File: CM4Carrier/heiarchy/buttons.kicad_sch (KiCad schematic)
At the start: 69 parts, among them J2 Conn_01x04_Female, SW1 SW_Push, SW10 SW_Push, SW11 SW_Push, SW2 SW_Push, SW3 SW_Push, SW4 SW_Push, SW5 SW_Push, SW6 SW_Push, SW7 SW_Push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

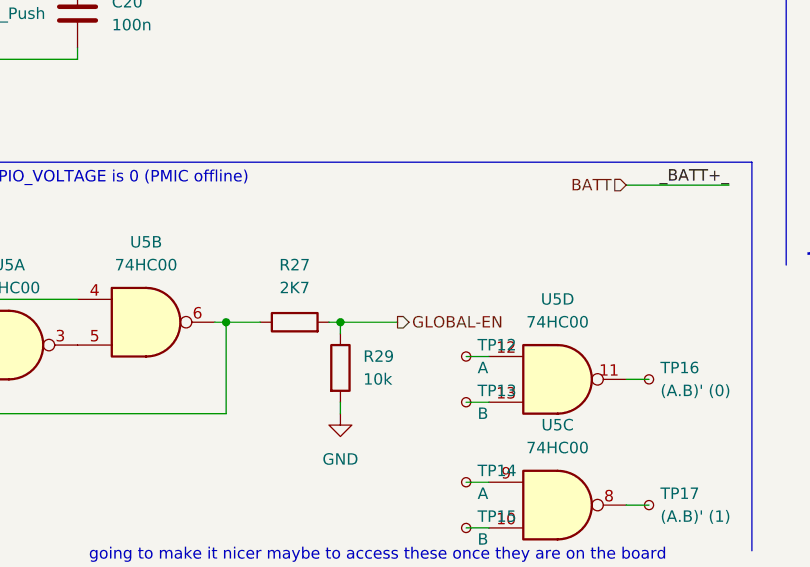
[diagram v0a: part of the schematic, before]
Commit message: PCB work
Home-stretch! Remaining things:
- Forgot Headphone jack / audio in design - add.
- route power supply (aaaaa)
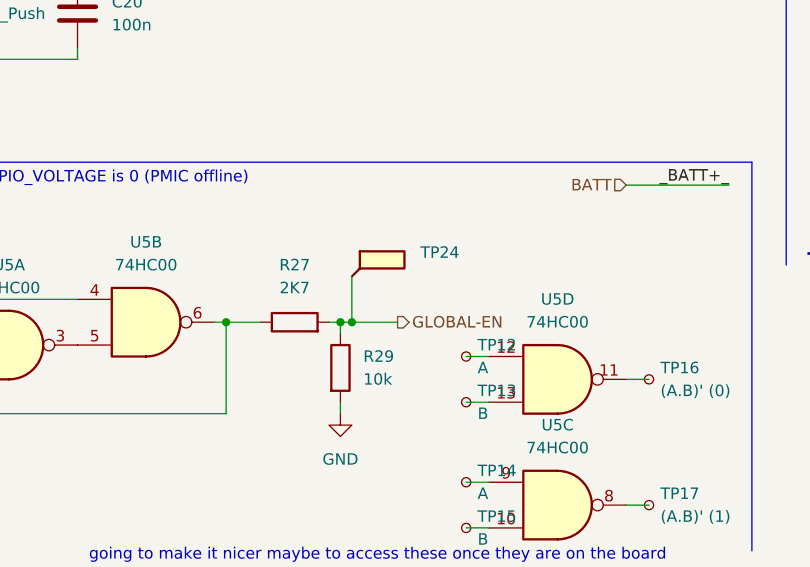
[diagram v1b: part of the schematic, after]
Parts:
- added TP24: (no value), symbol Connector:TestPoint_Flag
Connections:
- net GLOBAL-EN: now also TP24.1
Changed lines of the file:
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@@
   (junction (at 88.9 40.64) (diameter 0) (color 0 0 0 0)
   )
+  (junction (at 129.54 171.45) (diameter 0) (color 0 0 0 0)
+  )
   (junction (at 60.96 173.99) (diameter 0) (color 0 0 0 0)
   )
@@
     (stroke (width 0) (type default) (color 0 0 0 0))
   )
+  (wire (pts (xy 128.27 171.45) (xy 129.54 171.45))
+    (stroke (width 0) (type default) (color 0 0 0 0))
+  )
   (wire (pts (xy 88.9 40.64) (xy 88.9 39.37))
     (stroke (width 0) (type default) (color 0 0 0 0))
@@
     (stroke (width 0) (type default) (color 0 0 0 0))
   )
+  (wire (pts (xy 129.54 171.45) (xy 134.62 171.45))
+    (stroke (width 0) (type default) (color 0 0 0 0))
+  )
   (wire (pts (xy 111.76 76.2) (xy 114.3 76.2))
     (stroke (width 0) (type default) (color 0 0 0 0))
@@
     (stroke (width 0) (type default) (color 0 0 0 0))
   )
+  (wire (pts (xy 129.54 166.37) (xy 129.54 171.45))
+    (stroke (width 0) (type default) (color 0 0 0 0))
+  )
   (wire (pts (xy 142.24 189.23) (xy 144.78 189.23))
     (stroke (width 0) (type default) (color 0 0 0 0))
@@
   )
   (wire (pts (xy 204.47 45.72) (xy 204.47 46.99))
-    (stroke (width 0) (type default) (color 0 0 0 0))
-  )
-  (wire (pts (xy 128.27 171.45) (xy 134.62 171.45))
     (stroke (width 0) (type default) (color 0 0 0 0))
   )
@@
     (pin "1")
     (pin "2")
+  )
+  (symbol (lib_id "Connector:TestPoint_Flag") (at 129.54 166.37 0) (unit 1)
+    (in_bom yes) (on_board yes) (fields_autoplaced)
+    (property "Reference" "TP24" (id 0) (at 137.16 163.7029 0)
+      (effects (font (size 1.27 1.27)) (justify left))
+    )
+    (property "Value" "" (id 1) (at 137.16 166.2429 0)
+      (effects (font (size 1.27 1.27)) (justify left))
+    )
+    (property "Footprint" "" (id 2) (at 134.62 166.37 0)
+      (effects (font (size 1.27 1.27)) hide)
+    )
+    (property "Datasheet" "~" (id 3) (at 134.62 166.37 0)
+      (effects (font (size 1.27 1.27)) hide)
+    )
+    (pin "1")
   )
   (symbol (lib_id "Connector:TestPoint_Small") (at 142.24 189.23 0) (unit 1)
@@
       (effects (font (size 1.27 1.27)) hide)
     )
+    (pin "1")
+    (pin "2")
+    (pin "3")
+    (pin "4")
+    (pin "5")
+    (pin "6")
+    (pin "10")
+    (pin "8")
+    (pin "9")
+    (pin "11")
+    (pin "12")
+    (pin "13")
     (pin "14")
     (pin "7")
@@
       (effects (font (size 1.27 1.27)) hide)
     )
+    (pin "1")
+    (pin "2")
+    (pin "3")
     (pin "4")
     (pin "5")
     (pin "6")
+    (pin "10")
+    (pin "8")
+    (pin "9")
+    (pin "11")
+    (pin "12")
+    (pin "13")
+    (pin "14")
+    (pin "7")
   )
   (symbol (lib_id "Switch:SW_Push") (at 247.65 72.39 90) (unit 1)
@@
       (effects (font (size 1.27 1.27)) hide)
     )
+    (pin "1")
+    (pin "2")
+    (pin "3")
+    (pin "4")
+    (pin "5")
+    (pin "6")
     (pin "10")
     (pin "8")
     (pin "9")
+    (pin "11")
+    (pin "12")
+    (pin "13")
+    (pin "14")
+    (pin "7")
   )
   (symbol (lib_id "Connector:TestPoint_Flag") (at 134.62 63.5 0) (unit 1)
@@
       (effects (font (size 1.27 1.27)) hide)
     )
+    (pin "1")
+    (pin "2")
+    (pin "3")
+    (pin "4")
+    (pin "5")
+    (pin "6")
+    (pin "10")
+    (pin "8")
+    (pin "9")
     (pin "11")
     (pin "12")
     (pin "13")
+    (pin "14")
+    (pin "7")
   )
   (symbol (lib_id "Device:C") (at 88.9 97.79 0) (unit 1)
@@
     (pin "2")
     (pin "3")
+    (pin "4")
+    (pin "5")
+    (pin "6")
+    (pin "10")
+    (pin "8")
+    (pin "9")
+    (pin "11")
+    (pin "12")
+    (pin "13")
+    (pin "14")
+    (pin "7")
   )
 )

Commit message: LAYOUT DONE!!
:)
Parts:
- TP24: value (none) -> TP-GLOBALEN; footprint (none) -> TestPoint:TestPoint_THTPad_1.0x1.0mm_Drill0.5mm
- U5: value 74HC00 -> (none); footprint Package_DIP:DIP-14_W7.62mm_Socket_LongPads -> (none)
- U6: value MCP3002 -> (none); footprint Package_DIP:DIP-8_W7.62mm_LongPads -> (none)
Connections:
- net _BATT+ is gone; now on net BATT: R17.2, R19.2, U5.14 (VCC)
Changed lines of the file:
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@@
     (effects (font (size 2.54 2.54)) (justify left bottom))
   )
-  (label "_BATT+_" (at 171.45 156.21 180)
+  (label "BATT_S" (at 171.45 156.21 180)
     (effects (font (size 1.27 1.27)) (justify right bottom))
   )
@@
     (effects (font (size 1.27 1.27)) (justify left bottom))
   )
-  (label "_BATT+" (at 20.32 160.02 0)
+  (label "BATT_S" (at 20.32 160.02 0)
     (effects (font (size 1.27 1.27)) (justify left bottom))
   )
@@
     (effects (font (size 1.27 1.27)) (justify right bottom))
   )
-  (label "_BATT+" (at 69.85 158.75 180)
+  (label "BATT_S" (at 69.85 158.75 180)
     (effects (font (size 1.27 1.27)) (justify right bottom))
   )
@@
       (effects (font (size 1.27 1.27)) (justify left))
     )
-    (property "Value" "" (id 1) (at 137.16 166.2429 0)
-      (effects (font (size 1.27 1.27)) (justify left))
-    )
-    (property "Footprint" "" (id 2) (at 134.62 166.37 0)
+    (property "Value" "TP-GLOBALEN" (id 1) (at 137.16 166.2429 0)
+      (effects (font (size 1.27 1.27)) (justify left))
+    )
+    (property "Footprint" "TestPoint:TestPoint_THTPad_1.0x1.0mm_Drill0.5mm" (id 2) (at 134.62 166.37 0)
       (effects (font (size 1.27 1.27)) hide)
     )
@@
       (effects (font (size 1.27 1.27)) (justify left))
     )
-    (property "Value" "74HC00" (id 1) (at 31.75 175.2599 0)
-      (effects (font (size 1.27 1.27)) (justify left))
-    )
-    (property "Footprint" "Package_DIP:DIP-14_W7.62mm_Socket_LongPads" (id 2) (at 25.4 173.99 0)
-      (effects (font (size 1.27 1.27)) hide)
-    )
+    (property "Value" "" (id 1) (at 31.75 175.2599 0)
+      (effects (font (size 1.27 1.27)) (justify left))
+    )
+    (property "Footprint" "" (id 2) (at 25.4 173.99 0))
     (property "Datasheet" "http://www.ti.com/lit/gpn/sn74hc00" (id 3) (at 25.4 173.99 0)
       (effects (font (size 1.27 1.27)) hide)
@@
     (in_bom yes) (on_board yes) (fields_autoplaced)
     (property "Reference" "U5" (id 0) (at 106.68 162.56 0))
-    (property "Value" "74HC00" (id 1) (at 106.68 165.1 0))
-    (property "Footprint" "Package_DIP:DIP-14_W7.62mm_Socket_LongPads" (id 2) (at 106.68 171.45 0)
+    (property "Value" "" (id 1) (at 106.68 165.1 0))
+    (property "Footprint" "" (id 2) (at 106.68 171.45 0)
       (effects (font (size 1.27 1.27)) hide)
     )
@@
       (effects (font (size 1.27 1.27)) (justify left))
     )
-    (property "Value" "MCP3002" (id 1) (at 258.5594 116.84 0)
-      (effects (font (size 1.27 1.27)) (justify left))
-    )
-    (property "Footprint" "Package_DIP:DIP-8_W7.62mm_LongPads" (id 2) (at 256.54 132.08 0)
+    (property "Value" "" (id 1) (at 258.5594 116.84 0)
+      (effects (font (size 1.27 1.27)) (justify left))
+    )
+    (property "Footprint" "" (id 2) (at 256.54 132.08 0)
       (effects (font (size 1.27 1.27)) hide)
     )
@@
     (in_bom yes) (on_board yes) (fields_autoplaced)
     (property "Reference" "U5" (id 0) (at 152.4 182.88 0))
-    (property "Value" "74HC00" (id 1) (at 152.4 185.42 0))
-    (property "Footprint" "Package_DIP:DIP-14_W7.62mm_Socket_LongPads" (id 2) (at 152.4 191.77 0)
+    (property "Value" "" (id 1) (at 152.4 185.42 0))
+    (property "Footprint" "" (id 2) (at 152.4 191.77 0)
       (effects (font (size 1.27 1.27)) hide)
     )
@@
     (in_bom yes) (on_board yes) (fields_autoplaced)
     (property "Reference" "U5" (id 0) (at 152.4 168.91 0))
-    (property "Value" "74HC00" (id 1) (at 152.4 171.45 0))
-    (property "Footprint" "Package_DIP:DIP-14_W7.62mm_Socket_LongPads" (id 2) (at 152.4 177.8 0)
+    (property "Value" "" (id 1) (at 152.4 171.45 0))
+    (property "Footprint" "" (id 2) (at 152.4 177.8 0)
       (effects (font (size 1.27 1.27)) hide)
     )
@@
     (in_bom yes) (on_board yes) (fields_autoplaced)
     (property "Reference" "U5" (id 0) (at 91.44 165.1 0))
-    (property "Value" "74HC00" (id 1) (at 91.44 167.64 0))
-    (property "Footprint" "Package_DIP:DIP-14_W7.62mm_Socket_LongPads" (id 2) (at 91.44 173.99 0)
-      (effects (font (size 1.27 1.27)) hide)
-    )
+    (property "Value" "" (id 1) (at 91.44 167.64 0))
+    (property "Footprint" "" (id 2) (at 91.44 173.99 0)
+      (effects (font (size 1.27 1.27)) hide)
+    )

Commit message: fuseeeeeeeeeeeeeeeeeeeeeeeeeeeeeeeeeeeeeeeeeee
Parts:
- U5: value (none) -> 74HC00; footprint (none) -> Package_SO:SOIC-14_3.9x8.7mm_P1.27mm
- U6: value (none) -> MCP3002; footprint (none) -> Package_SO:TSSOP-8_4.4x3mm_P0.65mm
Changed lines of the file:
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@@
       (effects (font (size 1.27 1.27)) (justify left))
     )
-    (property "Value" "" (id 1) (at 31.75 175.2599 0)
-      (effects (font (size 1.27 1.27)) (justify left))
-    )
-    (property "Footprint" "" (id 2) (at 25.4 173.99 0))
+    (property "Value" "74HC00" (id 1) (at 31.75 175.2599 0)
+      (effects (font (size 1.27 1.27)) (justify left))
+    )
+    (property "Footprint" "Package_SO:SOIC-14_3.9x8.7mm_P1.27mm" (id 2) (at 25.4 173.99 0))
     (property "Datasheet" "http://www.ti.com/lit/gpn/sn74hc00" (id 3) (at 25.4 173.99 0)
       (effects (font (size 1.27 1.27)) hide)
@@
     (in_bom yes) (on_board yes) (fields_autoplaced)
     (property "Reference" "U5" (id 0) (at 106.68 162.56 0))
-    (property "Value" "" (id 1) (at 106.68 165.1 0))
-    (property "Footprint" "" (id 2) (at 106.68 171.45 0)
+    (property "Value" "74HC00" (id 1) (at 106.68 165.1 0))
+    (property "Footprint" "Package_SO:SOIC-14_3.9x8.7mm_P1.27mm" (id 2) (at 106.68 171.45 0)
       (effects (font (size 1.27 1.27)) hide)
     )
@@
       (effects (font (size 1.27 1.27)) (justify left))
     )
-    (property "Value" "" (id 1) (at 258.5594 116.84 0)
-      (effects (font (size 1.27 1.27)) (justify left))
-    )
-    (property "Footprint" "" (id 2) (at 256.54 132.08 0)
+    (property "Value" "MCP3002" (id 1) (at 258.5594 116.84 0)
+      (effects (font (size 1.27 1.27)) (justify left))
+    )
+    (property "Footprint" "Package_SO:TSSOP-8_4.4x3mm_P0.65mm" (id 2) (at 256.54 132.08 0)
       (effects (font (size 1.27 1.27)) hide)
     )
@@
     (in_bom yes) (on_board yes) (fields_autoplaced)
     (property "Reference" "U5" (id 0) (at 152.4 182.88 0))
-    (property "Value" "" (id 1) (at 152.4 185.42 0))
-    (property "Footprint" "" (id 2) (at 152.4 191.77 0)
+    (property "Value" "74HC00" (id 1) (at 152.4 185.42 0))
+    (property "Footprint" "Package_SO:SOIC-14_3.9x8.7mm_P1.27mm" (id 2) (at 152.4 191.77 0)
       (effects (font (size 1.27 1.27)) hide)
     )
@@
     (in_bom yes) (on_board yes) (fields_autoplaced)
     (property "Reference" "U5" (id 0) (at 152.4 168.91 0))
-    (property "Value" "" (id 1) (at 152.4 171.45 0))
-    (property "Footprint" "" (id 2) (at 152.4 177.8 0)
+    (property "Value" "74HC00" (id 1) (at 152.4 171.45 0))
+    (property "Footprint" "Package_SO:SOIC-14_3.9x8.7mm_P1.27mm" (id 2) (at 152.4 177.8 0)
       (effects (font (size 1.27 1.27)) hide)
     )
@@
     (in_bom yes) (on_board yes) (fields_autoplaced)
     (property "Reference" "U5" (id 0) (at 91.44 165.1 0))
-    (property "Value" "" (id 1) (at 91.44 167.64 0))
-    (property "Footprint" "" (id 2) (at 91.44 173.99 0)
-      (effects (font (size 1.27 1.27)) hide)
-    )
+    (property "Value" "74HC00" (id 1) (at 91.44 167.64 0))
+    (property "Footprint" "Package_SO:SOIC-14_3.9x8.7mm_P1.27mm" (id 2) (at 91.44 173.99 0)
+      (effects (font (size 1.27 1.27)) hide)
+    )

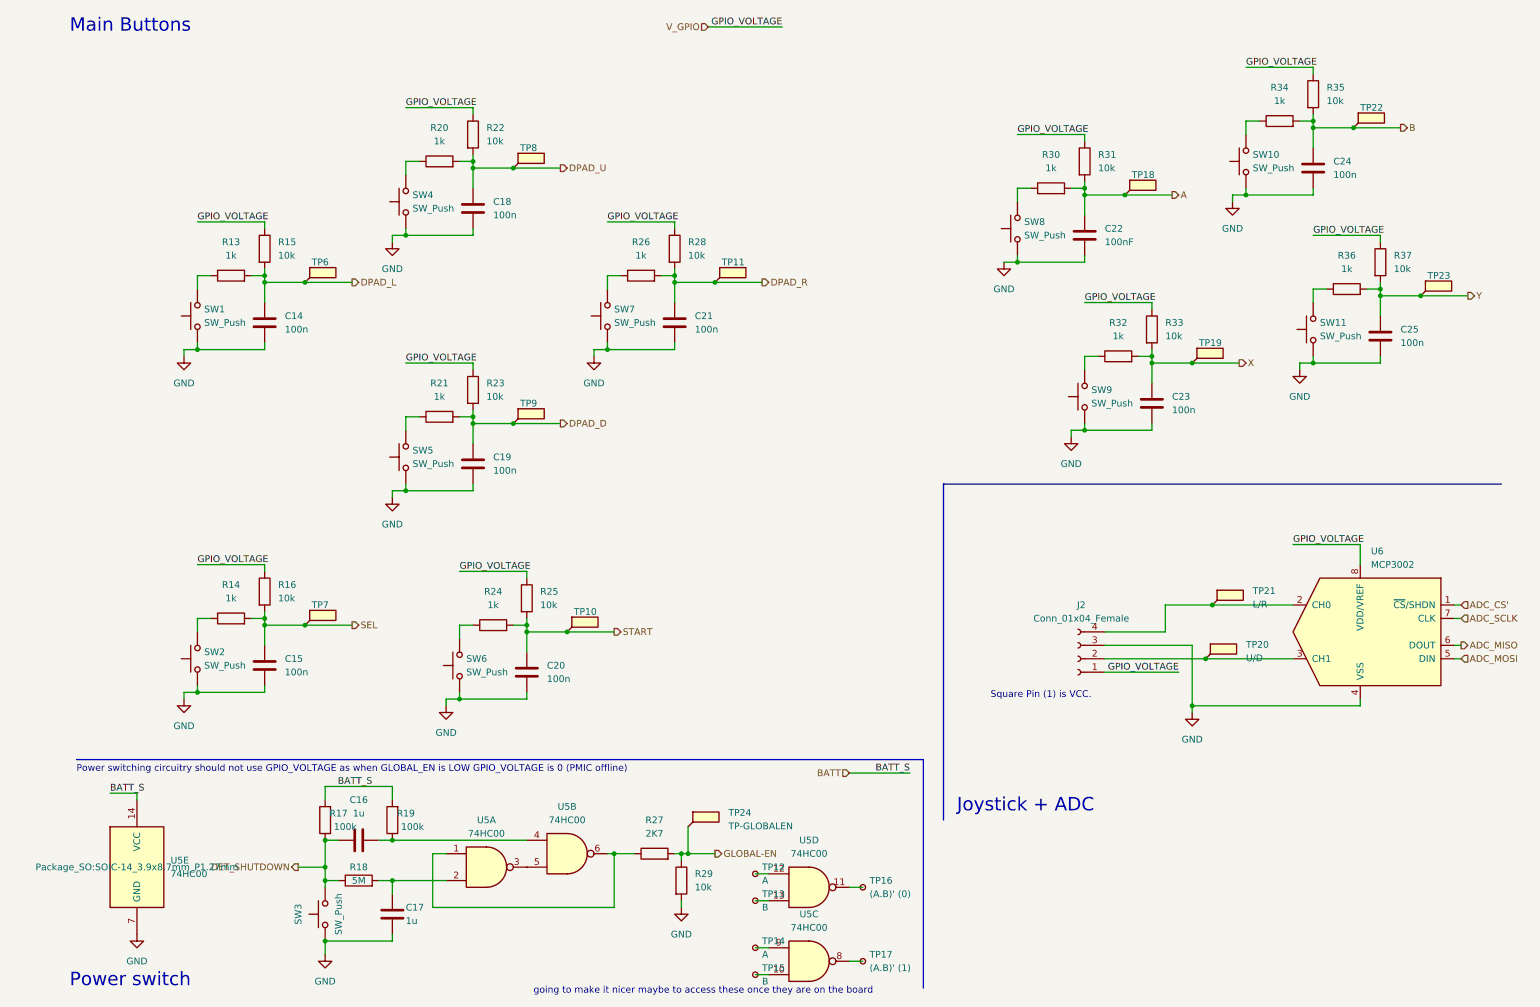
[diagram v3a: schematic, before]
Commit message: add buttons
need to adjust 3d model for buttons and add them to pcb... forgot about these.
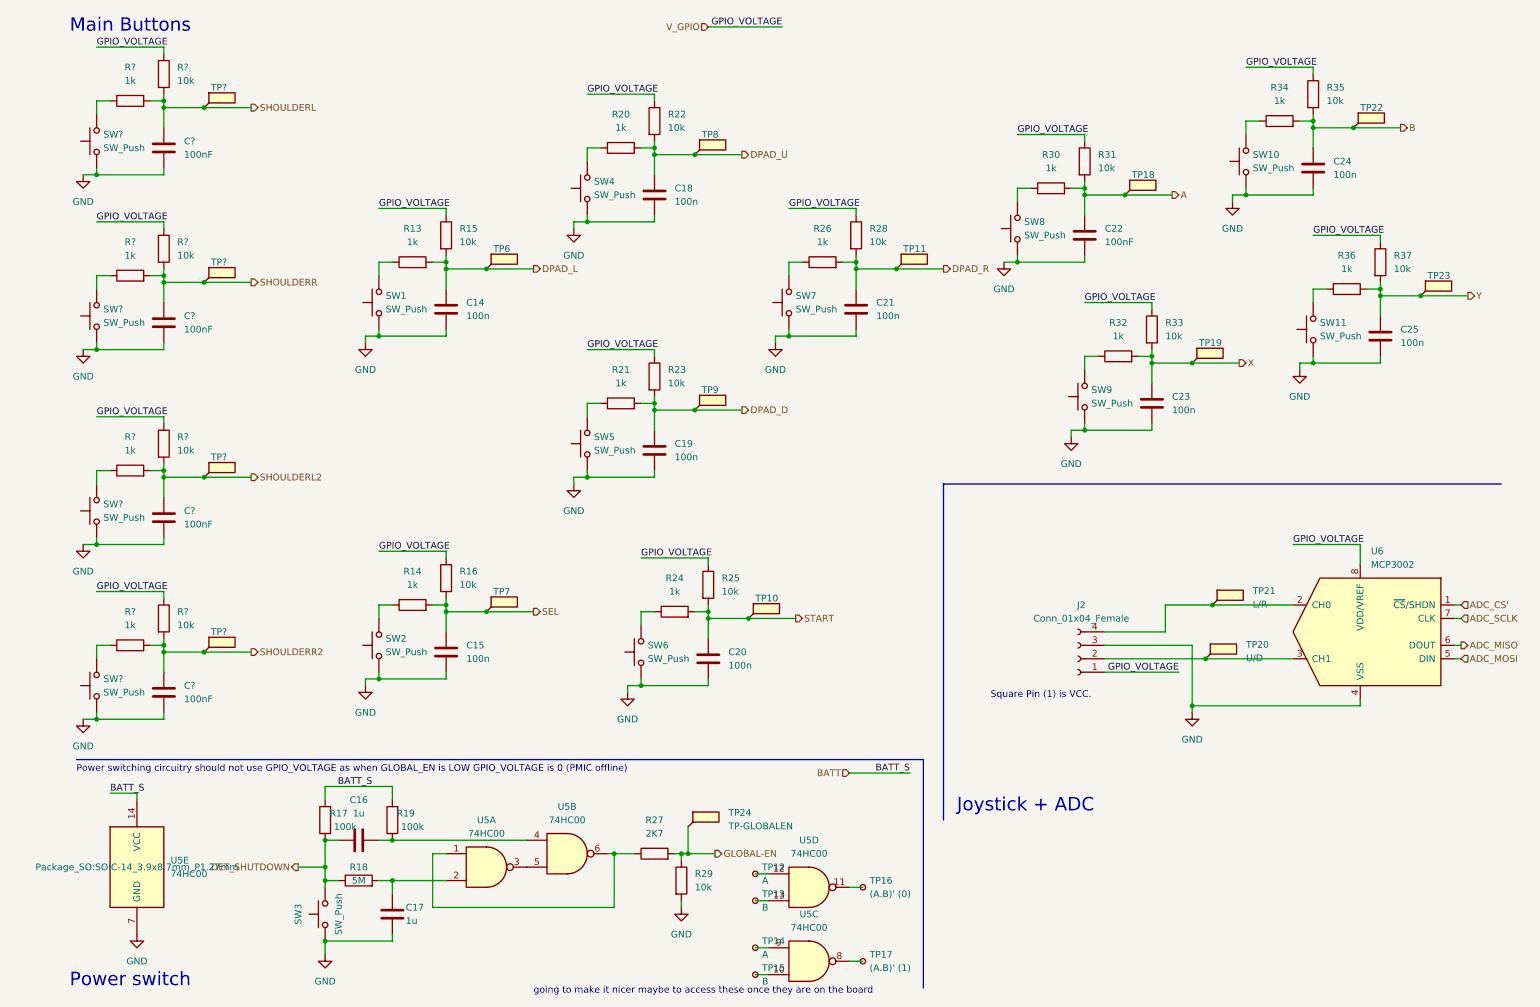
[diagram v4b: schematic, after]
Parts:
- added C? (x4): 100nF, Capacitor_SMD:C_0805_2012Metric_Pad1.18x1.45mm_HandSolder, symbol Device:C
- added R? (x4): 10k, Resistor_SMD:R_0805_2012Metric_Pad1.20x1.40mm_HandSolder, symbol Device:R
- added R? (x4): 1k, Resistor_SMD:R_0805_2012Metric_Pad1.20x1.40mm_HandSolder, symbol Device:R
- added SW? (x4): SW_Push, CM4IO:SW_PTS526_SMG15_SMTR2_LFS, symbol Switch:SW_Push
- added TP? (x4): A, TestPoint:TestPoint_THTPad_1.0x1.0mm_Drill0.5mm, symbol Connector:TestPoint_Flag
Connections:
- net GND: now also C?.2, C?.2, C?.2, C?.2, SW?.1, SW?.1, SW?.1, SW?.1
- net V_GPIO: now also R?.1, R?.1, R?.1, R?.1
- new net: R?.1, SW?.2 (x4)
- new net SHOULDERL: C?.1, R?.2, R?.2, TP?.1
- new net SHOULDERL2: C?.1, R?.2, R?.2, TP?.1
- new net SHOULDERR: C?.1, R?.2, R?.2, TP?.1
- new net SHOULDERR2: C?.1, R?.2, R?.2, TP?.1
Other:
- moved on the sheet: C14, C15, C18, C19, C20, C21, R13, R14, R15, R16, R20, R21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
